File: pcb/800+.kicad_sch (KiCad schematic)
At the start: 37 parts, among them J1 2inch LCD, J6 ESP_JTAG, J7 ESP_PROG, Q1 AO3401A, Q2 AO3401A, Q3 AO3401A, Q4 AO3401A, U12 VEML7700-TR, U2 ESP32-S3-WROOM-1U, U7 TSOP75340TT

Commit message: todo
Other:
- note added: "Design updates: ESP32 6 free GPIO MSP430 -2 free gpio Check reverse mount led footprint. Pads seem wider than needed. Connector and standard lipo battery for alternative ESP32 JTAG connector by the esp32, remove case to access MSP430 SWD to battery access cutout, more useful Rotate backlight led foot prints to maximize clearance to holes for better routing Add/fix courtyards to custom footprints 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"
- note removed: "Design updates: ESP32 6 free GPIO MSP430 -2 free gpio Connector and standard lipo battery for alternative ESP32 JTAG connector by the esp32, remove case to access MSP430 SWD to battery access cutout, more useful Rotate backlight led foot prints to maximize clearance to holes for better routing Add/fix courtyards to custom footprints Add mic to design? 3v3vp power enable pull down? Add inertial me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"
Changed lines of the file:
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@@
     (effects (font (size 1.27 1.27)) (justify left bottom))
   )
-  (text "Design updates:\n\nESP32 6 free GPIO\nMSP430 -2 free gpio\n\nConnector and standard lipo battery for alternative\n\nESP32 JTAG connector by the esp32, remove case to access\nMSP430 SWD to battery access cutout, more useful\n\nRotate backlight led foot prints to maximize clearance to holes for better routing\n\nAdd/fix courtyards to custom footprints\n\nAdd mic to design?\n\n3v3vp power enable pull down?\n\nAdd inertial measurement, tilt shake tap remote as user inputs\n\nUpdate cradle footprint to support stock and generic jst 1.25\nbattery thermistor, find way to pulse or control supply current\nvref from msp430, one of the port 2 inputs switched briefly.\n\nIs ESP TX to MSP needed?  Removed it, we will see....\nRolling ball might work as last switch on button matrix\n\nRegular LEDs instead of reverse mount, \n--less holes and cheaper, clearance and 2 reflows.  Tape to mount switch domes more complicated\n--1206 upside down, cheaper, 1 reflow, more hand rework\n--SK6812Mini reverse mount, cheap, but bigger cutout battery compartment clearance\n--Leds on flex PCB attached to main PCB like the stock EL\n\nDielectric grease on dome switches.  Hold in place until taped, prevent corrosion but messy\n\nSoftware:\nTest energeia/Arduino on MSP430 vs bare metal\n\nTest:\npower supply operation and feedback\nambient light sensor operation inside case.\nIR input and output\nIR output LED performance\nAlternate rolling ball for better response\nBattery charging\nFuel gauge\nBuzzer\nPower consumption\nAustralian power adapter looks like 5.5v vs 8v for us\n\nOrder:\nJST connector from DigiKey\nTranslucent white tape to diffuse leds\n\nAliExpress 2.5mm x 5p connector fits battery snuggly, too short\nkeep looking for available replacements\n"
+  (text "Design updates:\n\nESP32 6 free GPIO\nMSP430 -2 free gpio\n\nCheck reverse mount led footprint.  Pads seem wider than needed.\n\nConnector and standard lipo battery for alternative\n\nESP32 JTAG connector by the esp32, remove case to access\nMSP430 SWD to battery access cutout, more useful\n\nRotate backlight led foot prints to maximize clearance to holes for better routing\n\nAdd/fix courtyards to custom footprints\n\nAdd mic to design?\n\nLC709203F for fuel gauge, integrated temp sense\n\n3v3vp power enable pull down?\n\nAdd inertial measurement, tilt shake tap remote as user inputs\n\nUpdate cradle footprint to support stock and generic jst 1.25\nbattery thermistor, find way to pulse or control supply current\nvref from msp430, one of the port 2 inputs switched briefly.\n\nIs ESP TX to MSP needed?  Removed it, we will see....\nRolling ball might work as last switch on button matrix\n\nRegular LEDs instead of reverse mount, \n--less holes and cheaper, clearance and 2 reflows.  Tape to mount switch domes more complicated\n--1206 upside down, cheaper, 1 reflow, more hand rework\n--SK6812Mini reverse mount, cheap, but bigger cutout battery compartment clearance\n--Leds on flex PCB attached to main PCB like the stock EL\n\nDielectric grease on dome switches.  Hold in place until taped, prevent corrosion but messy\n\nSoftware:\nTest energeia/Arduino on MSP430 vs bare metal\n\nTest:\npower supply operation and feedback\nambient light sensor operation inside case.\nIR input and output\nIR output LED performance\nAlternate rolling ball for better response\nBattery charging\nFuel gauge\nBuzzer\nPower consumption\nAustralian power adapter looks like 5.5v vs 8v for us\n\nOrder:\nJST connector from DigiKey\nLC709203F\nTranslucent white tape to diffuse leds\n\nAliExpress 2.5mm x 5p connector fits battery snuggly, ordered a few\n"
     (at 30.48 331.47 0)
     (effects (font (size 1.27 1.27)) (justify left bottom))

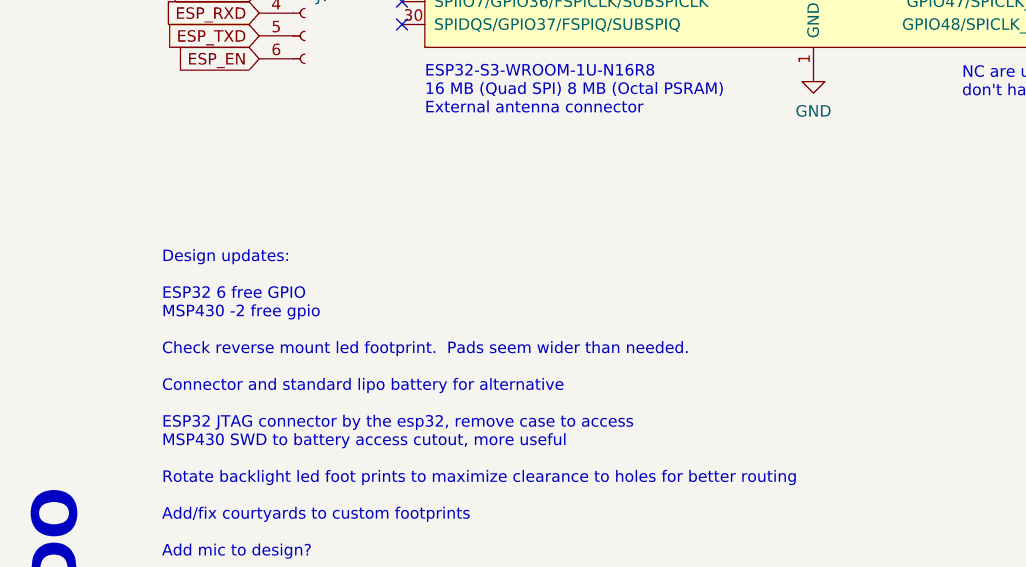
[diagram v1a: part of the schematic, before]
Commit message: IR led fix
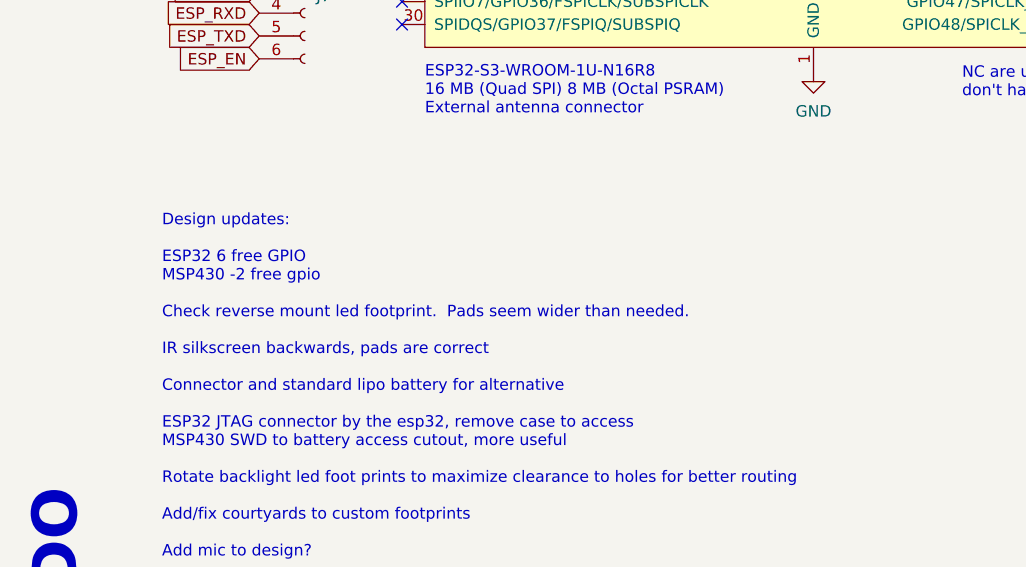
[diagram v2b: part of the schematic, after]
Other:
- note added: "Design updates: ESP32 6 free GPIO MSP430 -2 free gpio Check reverse mount led footprint. Pads seem wider than needed. IR silkscreen backwards, pads are correct Connector and standard lipo battery for alternative ESP32 JTAG connector by the esp32, remove case to access MSP430 SWD to battery access cutout, more useful Rotate backlight led foot prints to maximize clearance to holes for better routin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"
- note removed: "Design updates: ESP32 6 free GPIO MSP430 -2 free gpio Check reverse mount led footprint. Pads seem wider than needed. Connector and standard lipo battery for alternative ESP32 JTAG connector by the esp32, remove case to access MSP430 SWD to battery access cutout, more useful Rotate backlight led foot prints to maximize clearance to holes for better routing Add/fix courtyards to custom footprints 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"
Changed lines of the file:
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@@
     (effects (font (size 1.27 1.27)) (justify left bottom))
   )
-  (text "Design updates:\n\nESP32 6 free GPIO\nMSP430 -2 free gpio\n\nCheck reverse mount led footprint.  Pads seem wider than needed.\n\nConnector and standard lipo battery for alternative\n\nESP32 JTAG connector by the esp32, remove case to access\nMSP430 SWD to battery access cutout, more useful\n\nRotate backlight led foot prints to maximize clearance to holes for better routing\n\nAdd/fix courtyards to custom footprints\n\nAdd mic to design?\n\nLC709203F for fuel gauge, integrated temp sense\n\n3v3vp power enable pull down?\n\nAdd inertial measurement, tilt shake tap remote as user inputs\n\nUpdate cradle footprint to support stock and generic jst 1.25\nbattery thermistor, find way to pulse or control supply current\nvref from msp430, one of the port 2 inputs switched briefly.\n\nIs ESP TX to MSP needed?  Removed it, we will see....\nRolling ball might work as last switch on button matrix\n\nRegular LEDs instead of reverse mount, \n--less holes and cheaper, clearance and 2 reflows.  Tape to mount switch domes more complicated\n--1206 upside down, cheaper, 1 reflow, more hand rework\n--SK6812Mini reverse mount, cheap, but bigger cutout battery compartment clearance\n--Leds on flex PCB attached to main PCB like the stock EL\n\nDielectric grease on dome switches.  Hold in place until taped, prevent corrosion but messy\n\nSoftware:\nTest energeia/Arduino on MSP430 vs bare metal\n\nTest:\npower supply operation and feedback\nambient light sensor operation inside case.\nIR input and output\nIR output LED performance\nAlternate rolling ball for better response\nBattery charging\nFuel gauge\nBuzzer\nPower consumption\nAustralian power adapter looks like 5.5v vs 8v for us\n\nOrder:\nJST connector from DigiKey\nLC709203F\nTranslucent white tape to diffuse leds\n\nAliExpress 2.5mm x 5p connector fits battery snuggly, ordered a few\n"
+  (text "Design updates:\n\nESP32 6 free GPIO\nMSP430 -2 free gpio\n\nCheck reverse mount led footprint.  Pads seem wider than needed.\n\nIR silkscreen backwards, pads are correct\n\nConnector and standard lipo battery for alternative\n\nESP32 JTAG connector by the esp32, remove case to access\nMSP430 SWD to battery access cutout, more useful\n\nRotate backlight led foot prints to maximize clearance to holes for better routing\n\nAdd/fix courtyards to custom footprints\n\nAdd mic to design?\n\nLC709203F for fuel gauge, integrated temp sense\n\n3v3vp power enable pull down?\n\nAdd inertial measurement, tilt shake tap remote as user inputs\n\nUpdate cradle footprint to support stock and generic jst 1.25\nbattery thermistor, find way to pulse or control supply current\nvref from msp430, one of the port 2 inputs switched briefly.\n\nIs ESP TX to MSP needed?  Removed it, we will see....\nRolling ball might work as last switch on button matrix\n\nRegular LEDs instead of reverse mount, \n--less holes and cheaper, clearance and 2 reflows.  Tape to mount switch domes more complicated\n--1206 upside down, cheaper, 1 reflow, more hand rework\n--SK6812Mini reverse mount, cheap, but bigger cutout battery compartment clearance\n--Leds on flex PCB attached to main PCB like the stock EL\n\nDielectric grease on dome switches.  Hold in place until taped, prevent corrosion but messy\n\nSoftware:\nTest energeia/Arduino on MSP430 vs bare metal\n\nTest:\npower supply operation and feedback\nambient light sensor operation inside case.\nIR input and output\nIR output LED performance\nAlternate rolling ball for better response\nBattery charging\nFuel gauge\nBuzzer\nPower consumption\nAustralian power adapter looks like 5.5v vs 8v for us\n\nOrder:\nJST connector from DigiKey\nLC709203F\nTranslucent white tape to diffuse leds\n\nAliExpress 2.5mm x 5p connector fits battery snuggly, ordered a few\n"
     (at 30.48 331.47 0)
     (effects (font (size 1.27 1.27)) (justify left bottom))

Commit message: lux and buzzer
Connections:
- net ESP_TO_MSP: now also U2.10 (GPIO17/U1TXD/ADC2_CH6)
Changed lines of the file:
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@@
     )
   )
-  (global_label "ESP_TO_MSP" (shape input) (at 168.91 161.925 0) (fields_autoplaced)
+  (global_label "ESP_TO_MSP" (shape input) (at 157.48 166.37 0) (fields_autoplaced)
     (effects (font (size 1.27 1.27)) (justify left))
-    (property "Intersheetrefs" "${INTERSHEET_REFS}" (at 183.6085 161.925 0)
+    (property "Intersheetrefs" "${INTERSHEET_REFS}" (at 172.1785 166.37 0)
       (effects (font (size 1.27 1.27)) (justify left) hide)
     )
